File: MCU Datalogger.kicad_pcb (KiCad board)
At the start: 2 copper layers, 50 x 30 mm, 30 parts, among them J1 Conn_01x09_Male, J2 Conn_01x04_Male, J3 Conn_02x03_Odd_Even, J4 Conn_01x04_Male, U1 24LC1025, U2 DS1337S+, U3 24LC1025, U4 ATMEGA328P-AU, Y1 32.768 KHz, Y2 16MHz

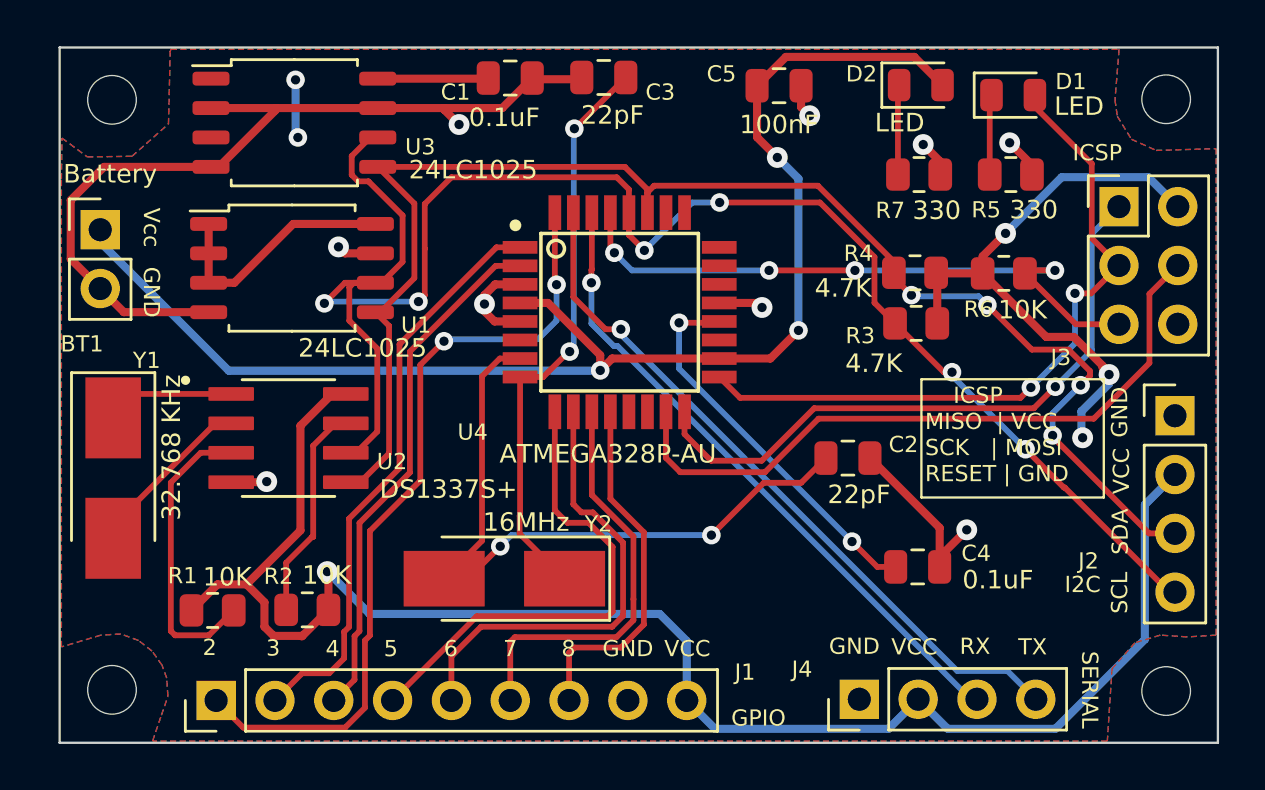
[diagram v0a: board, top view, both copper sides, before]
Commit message: more 4layer routing
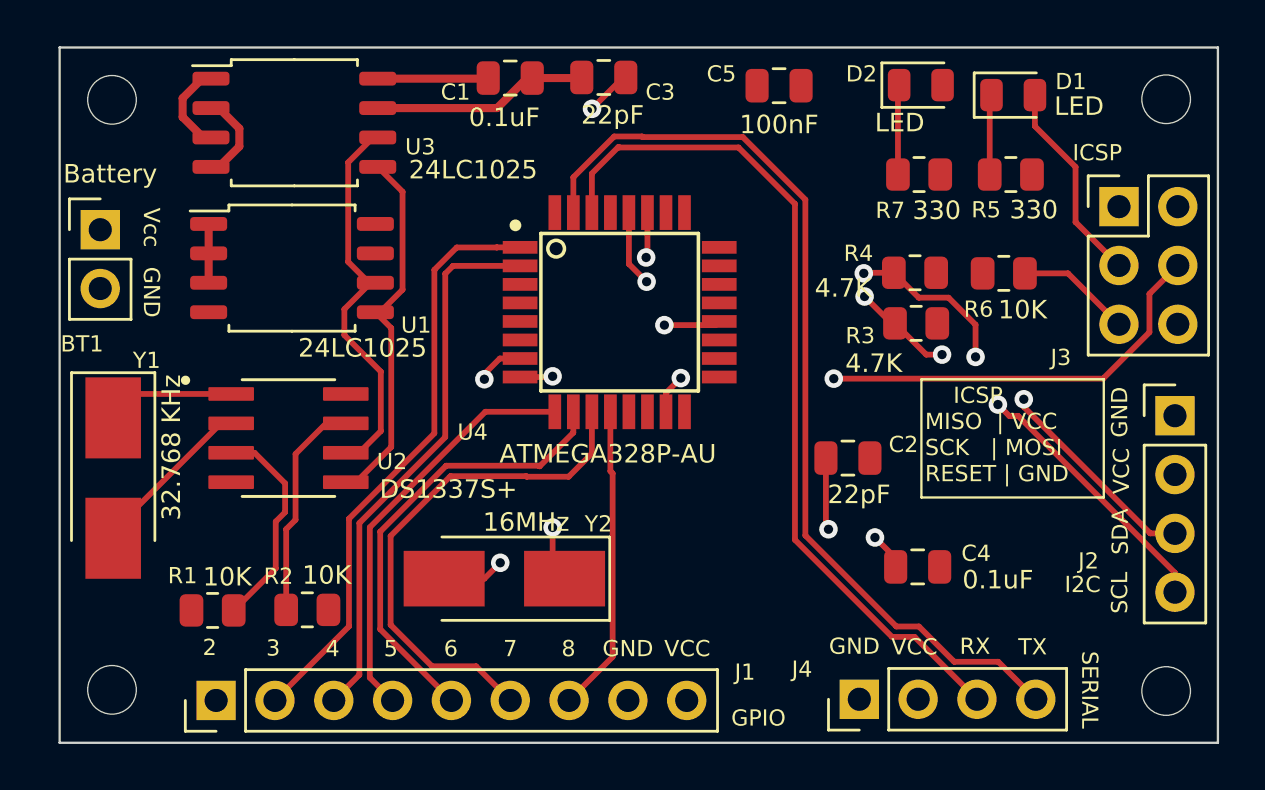
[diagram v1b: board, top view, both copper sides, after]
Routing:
- net /Vcc: track 173.5 -> 11.3 mm, vias 9 -> 0
- net GND: track 59.7 -> 13.3 mm, vias 9 -> 0
- net /D2: track 34.4 -> 0.00 mm, vias 2 -> 0
- net /MISO: track 27.7 -> 0.00 mm, vias 1 -> 0
- net /SCL: track 73.8 -> 49.4 mm, vias 6 -> 4
- net /RESET: track 27.5 -> 4.97 mm, vias 4 -> 0
- net /SCK: track 30.1 -> 8.86 mm, vias 2 -> 0
- net /SDA: track 63.9 -> 46.8 mm
- net /TX: track 30.9 -> 40.8 mm, vias 1 -> 0
- net /RX: track 28.2 -> 37.2 mm, vias 1 -> 0
- net /D7: track 18.0 -> 22.3 mm
- net /MOSI: track 29.8 -> 26.2 mm, vias 0 -> 2
- net Net-(R1-Pad2): track 12.8 -> 9.28 mm
- net /D5: track 21.3 -> 17.9 mm
- net /D8: track 15.6 -> 13.3 mm
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- removed copper zone on F.Cu, net /Vcc
- removed copper zone on B.Cu, net GND
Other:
- copper layers 2 -> 4

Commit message: more routing. Fills
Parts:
- moved Y2 2.78 mm to (100.2, 99.6)
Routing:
- net /D2: track 0.00 -> 31.2 mm
- net /Vcc: track 11.3 -> 34.9 mm, vias 0 -> 13
- net /RESET: track 4.97 -> 27.1 mm, vias 0 -> 2
- net GND: track 13.3 -> 35.3 mm, vias 0 -> 12
- net /SCL: track 49.4 -> 68.9 mm, vias 4 -> 6
- net /SDA: track 46.8 -> 61.4 mm, vias 4 -> 6
- net /D7: track 22.3 -> 16.2 mm
- net /D6: track 19.6 -> 15.2 mm
- net Net-(C3-Pad2): track 24.6 -> 27.9 mm
- net /D5: track 17.9 -> 15.4 mm
- net Net-(C2-Pad2): track 30.9 -> 29.0 mm
- net /D3: track 25.5 -> 26.4 mm
- net /D4: track 23.8 -> 23.1 mm
- added copper zone on B.Cu, net /Vcc
- added copper zone on In2.Cu, net /Vcc
- added copper zone on B.Cu, net GND

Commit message: routing good to go, copper fill good to go for 4layer version
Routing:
- net /MISO: track 0.00 -> 22.4 mm, vias 0 -> 1
- net /SCK: track 8.86 -> 29.4 mm, vias 0 -> 3
- net /MOSI: track 26.2 -> 27.9 mm
- net Net-(C4-Pad2): track 18.5 -> 19.8 mm
- removed copper zone on B.Cu, net /Vcc

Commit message: 4-layer is ready for manufacuturing
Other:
- board text added: "4.6900 mm"
- board text removed: "1.6000 mm"
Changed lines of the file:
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@@
       (drillshape 0)
       (scaleselection 1)
-      (outputdirectory "MCU_Datalogger_Gerbers/")
+      (outputdirectory "4-layer_MCU_Datalogger_Gerbers/")
     )
   )
@@
     (effects (font (size 0.7 0.7) (thickness 0.1)))
   )
-  (gr_text "1.6000 mm" (at 223.931543 82.4716) (layer "User.1")
+  (gr_text "No" (at 165.807143 101.245) (layer "User.1")
     (effects (font (size 1.5 1.5) (thickness 0.2)) (justify left top))
   )
-  (gr_text "50.1126 mm x 30.1228 mm" (at 165.031543 86.9866) (layer "User.1")
+  (gr_text "4" (at 165.807143 78.67) (layer "User.1")
     (effects (font (size 1.5 1.5) (thickness 0.2)) (justify left top))
   )
-  (gr_text "BOARD CHARACTERISTICS" (at 131.7244 76.3016) (layer "User.1")
-    (effects (font (size 2 2) (thickness 0.4)) (justify left top))
-  )
-  (gr_text "No" (at 223.931543 100.5316) (layer "User.1")
+  (gr_text "Impedance Control: " (at 199.864286 92.215) (layer "User.1")
     (effects (font (size 1.5 1.5) (thickness 0.2)) (justify left top))
   )
-  (gr_text "None" (at 165.031543 96.0166) (layer "User.1")
+  (gr_text "No" (at 224.707143 92.215) (layer "User.1")
     (effects (font (size 1.5 1.5) (thickness 0.2)) (justify left top))
   )
-  (gr_text "Edge card connectors: " (at 132.4744 105.0466) (layer "User.1")
+  (gr_text "No" (at 165.807143 96.73) (layer "User.1")
     (effects (font (size 1.5 1.5) (thickness 0.2)) (justify left top))
   )
-  (gr_text "Copper Finish: " (at 132.4744 96.0166) (layer "User.1")
+  (gr_text "50.1126 mm x 30.1228 mm" (at 165.807143 83.185) (layer "User.1")
     (effects (font (size 1.5 1.5) (thickness 0.2)) (justify left top))
   )
-  (gr_text "Plated Board Edge: " (at 199.088686 100.5316) (layer "User.1")
+  (gr_text "Copper Layer Count: " (at 133.25 78.67) (layer "User.1")
     (effects (font (size 1.5 1.5) (thickness 0.2)) (justify left top))
   )
-  (gr_text "0.3000 mm" (at 223.931543 91.5016) (layer "User.1")
+  (gr_text "Board overall dimensions: " (at 133.25 83.185) (layer "User.1")
     (effects (font (size 1.5 1.5) (thickness 0.2)) (justify left top))
   )
-  (gr_text "No" (at 223.931543 96.0166) (layer "User.1")
+  (gr_text "0.2000 mm / 0.0000 mm" (at 165.807143 87.7) (layer "User.1")
     (effects (font (size 1.5 1.5) (thickness 0.2)) (justify left top))
   )
-  (gr_text "Min track/spacing: " (at 132.4744 91.5016) (layer "User.1")
+  (gr_text "" (at 199.864286 83.185) (layer "User.1")
     (effects (font (size 1.5 1.5) (thickness 0.2)) (justify left top))
   )
-  (gr_text "No" (at 165.031543 105.0466) (layer "User.1")
+  (gr_text "0.3000 mm" (at 224.707143 87.7) (layer "User.1")
     (effects (font (size 1.5 1.5) (thickness 0.2)) (justify left top))
   )
-  (gr_text "0.2000 mm / 0.0000 mm" (at 165.031543 91.5016) (layer "User.1")
+  (gr_text "None" (at 165.807143 92.215) (layer "User.1")
     (effects (font (size 1.5 1.5) (thickness 0.2)) (justify left top))
   )
-  (gr_text "" (at 199.088686 86.9866) (layer "User.1")
+  (gr_text "Copper Finish: " (at 133.25 92.215) (layer "User.1")
     (effects (font (size 1.5 1.5) (thickness 0.2)) (justify left top))
   )
-  (gr_text "No" (at 165.031543 100.5316) (layer "User.1")
+  (gr_text "Castellated pads: " (at 133.25 96.73) (layer "User.1")
     (effects (font (size 1.5 1.5) (thickness 0.2)) (justify left top))
   )
-  (gr_text "Board overall dimensions: " (at 132.4744 86.9866) (layer "User.1")
+  (gr_text "Board Thickness: " (at 199.864286 78.67) (layer "User.1")
     (effects (font (size 1.5 1.5) (thickness 0.2)) (justify left top))
   )
-  (gr_text "Board Thickness: " (at 199.088686 82.4716) (layer "User.1")
+  (gr_text "BOARD CHARACTERISTICS" (at 132.5 72.5) (layer "User.1")
+    (effects (font (size 2 2) (thickness 0.4)) (justify left top))
+  )
+  (gr_text "" (at 224.707143 83.185) (layer "User.1")
     (effects (font (size 1.5 1.5) (thickness 0.2)) (justify left top))
   )
-  (gr_text "Impedance Control: " (at 199.088686 96.0166) (layer "User.1")
+  (gr_text "Min track/spacing: " (at 133.25 87.7) (layer "User.1")
     (effects (font (size 1.5 1.5) (thickness 0.2)) (justify left top))
   )
-  (gr_text "2" (at 165.031543 82.4716) (layer "User.1")
+  (gr_text "Edge card connectors: " (at 133.25 101.245) (layer "User.1")
     (effects (font (size 1.5 1.5) (thickness 0.2)) (justify left top))
   )
-  (gr_text "Copper Layer Count: " (at 132.4744 82.4716) (layer "User.1")
+  (gr_text "Plated Board Edge: " (at 199.864286 96.73) (layer "User.1")
     (effects (font (size 1.5 1.5) (thickness 0.2)) (justify left top))
   )
-  (gr_text "Castellated pads: " (at 132.4744 100.5316) (layer "User.1")
+  (gr_text "No" (at 224.707143 96.73) (layer "User.1")
     (effects (font (size 1.5 1.5) (thickness 0.2)) (justify left top))
   )
-  (gr_text "Min hole diameter: " (at 199.088686 91.5016) (layer "User.1")
+  (gr_text "4.6900 mm" (at 224.707143 78.67) (layer "User.1")
     (effects (font (size 1.5 1.5) (thickness 0.2)) (justify left top))
   )
-  (gr_text "" (at 223.931543 86.9866) (layer "User.1")
+  (gr_text "Min hole diameter: " (at 199.864286 87.7) (layer "User.1")
     (effects (font (size 1.5 1.5) (thickness 0.2)) (justify left top))
   )
@@
     )
   )
-  (group "group-boardCharacteristics" (id e50027c8-3f55-47be-85d7-0905666b13a4)
+  (group "group-boardCharacteristics" (id 269b46ae-8653-428f-a2c6-c787478ae3ef)
     (members
-      00946e54-e23a-466e-aae5-2589a54ba8c1
-      0770d3bb-648e-44fb-a285-7011409d7e3f
-      27381990-470e-4a26-8f9d-160290b54264
-      286551bb-e82f-49d5-bb5b-d3e43ccee387
-      2a698e19-d1b4-4900-ab45-156c58bbe22c
-      2c20bed1-9919-4abc-b755-a19a52c66fab
-      2e36f2b4-fc97-4923-b0b1-aba69dab0384
-      33829a50-77c4-4643-8088-001741518982
-      3b4fbe2e-70e6-4940-9c7f-e689491ef211
-      3f17a494-dfac-4cda-8891-a4cba449ce98
-      61446237-ea0d-4970-aec1-cbc03a3ab68b
-      69586585-dce2-48ca-b7db-bfd1b3ebf3d2
-      78aa8c32-9ae8-4411-8ffb-b688bce6f519
-      80806f0f-5680-4568-9c17-9cfe96f77875
-      80d5b919-4eb1-4ad6-a683-814af6c536b4
-      afd7ba8f-efbd-422a-846e-30a55ac71e09
-      b5c5a79b-9605-4548-9912-d982d1f17da0
-      bdb7c51c-a446-4625-8175-c513223d2009
-      c5d28a7c-88ba-4bdd-9eb9-ac6fdd03bb5a
-      d11d6b24-9684-4a0d-a9c2-082b3ed4c1c4
-      f47098fd-dd17-4651-a873-0bbc199951da
-      f476ec63-ec60-4ab5-969e-3c6bed46bd19
-      f6181fd0-9d8c-4e81-8303-1a88408e9e5c
+      056ef229-1a52-4bdd-b9bd-6353e3cbaae0
+      16aea607-1633-48a7-9f26-b897fdde3c77
+      1a0d999f-c151-4778-923e-9bbad61b8527
+      2ef6e57a-b83e-4cdf-8226-921f2e4417f3
+      30db0c04-9af6-4b10-b5ae-17bba5731a7d
+      3c26703d-1bbb-494d-8012-9ef86a506a96
+      3ee67041-ab91-448b-94c4-5883473bba58
+      459d2a77-f14c-438c-a318-d48d3641b8ca
+      5602a576-3b9b-4df0-a1c7-5b807859d478
+      58b2c4b6-d78a-4096-8d68-c56761433527
+      781e5835-8e2c-4548-a0ce-d2c36a03de9e
+      7dd74b6f-c08f-4a1f-a71d-8ea9cc271b6c
+      7f39f018-7b76-405e-a9ce-1ed597114184
+      80d41ae5-cd67-416e-8dbf-9bbfb978116a
+      94747bc7-8b46-4c1e-96f9-4b3c784f9ea3
+      98911611-c1c4-4b0a-bfee-581204c2e9d7
+      9cc71620-e206-43ac-876b-9f94c1b86e06
+      b1700c45-44ff-4d9a-95bb-656004091816
+      b29eb734-aa64-4e79-b8fc-cefe8bded78b
+      ba8f53a3-40ca-45d6-ba11-eb02f24c65a0
+      cf77819b-6e4f-42d2-91e9-2a18952983d5
+      df4da9f3-290a-4704-9fc8-f15e29058f17
+      fd1d6069-753e-4dfd-8e16-e9de65bad465
     )
   )
